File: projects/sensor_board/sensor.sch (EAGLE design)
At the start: 63 parts, among them J1 504050-0791, J2 FH28-10S-0.5SH_05_, J3 504050-0791, J4 504050-1091, J5 504050-0791, J6 504050-0791, U1 NXP_FXAS21002CQR1_EDITEDNXP_F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, U2 HONEYWELL_HMC5983-TRHONEYWELL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, U3 DS1307N, U4 NXP_FXAS21002CQR1_EDITEDNXP_F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, U5 HONEYWELL_HMC5983-TRHONEYWELL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, U6 NXP_FXAS21002CQR1_EDITEDNXP_F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, U7 HONEYWELL_HMC5983-TRHONEYWELL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, Y1 ECS-.327-12.5-13X

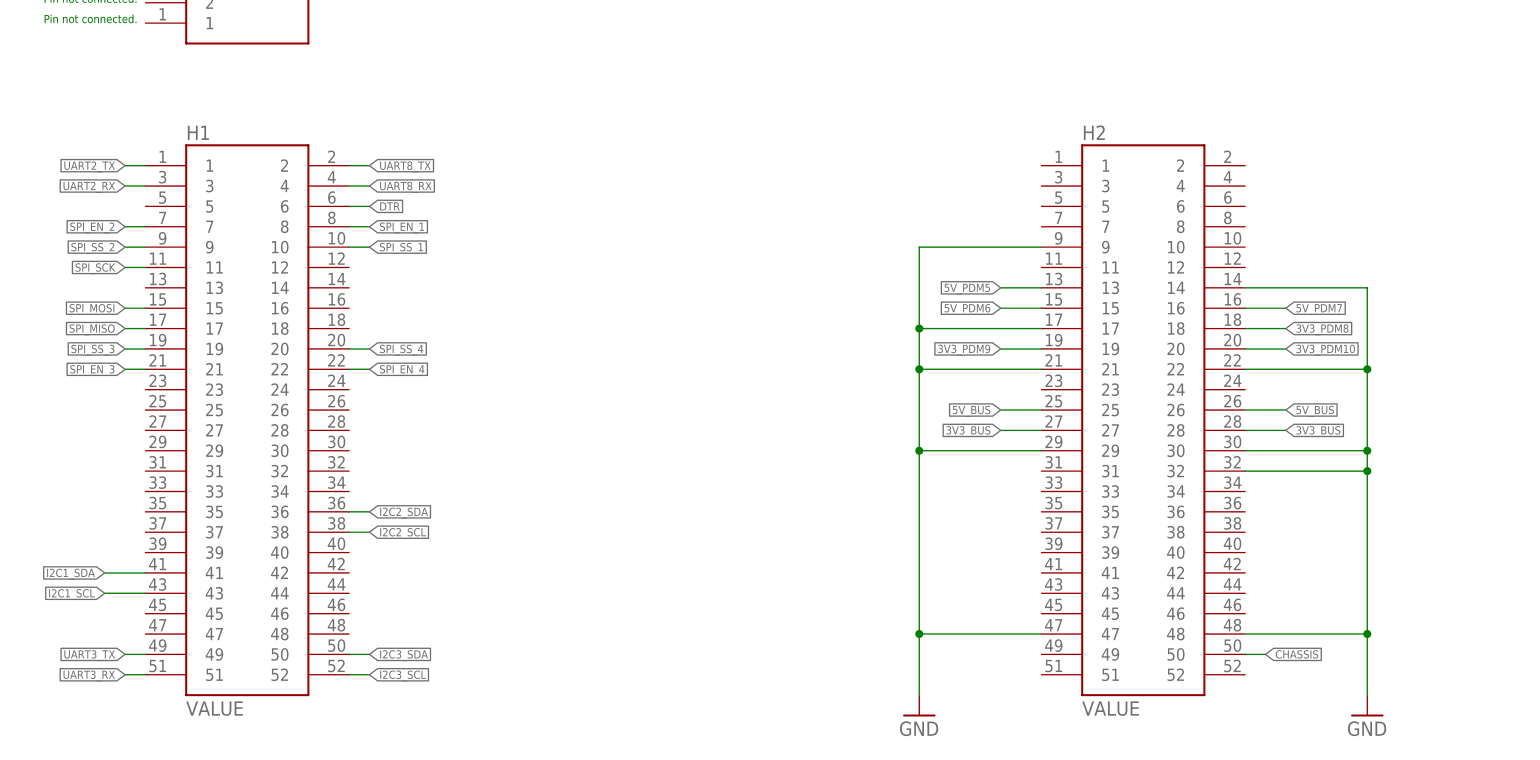
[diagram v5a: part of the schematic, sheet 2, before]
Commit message: sensor board updated
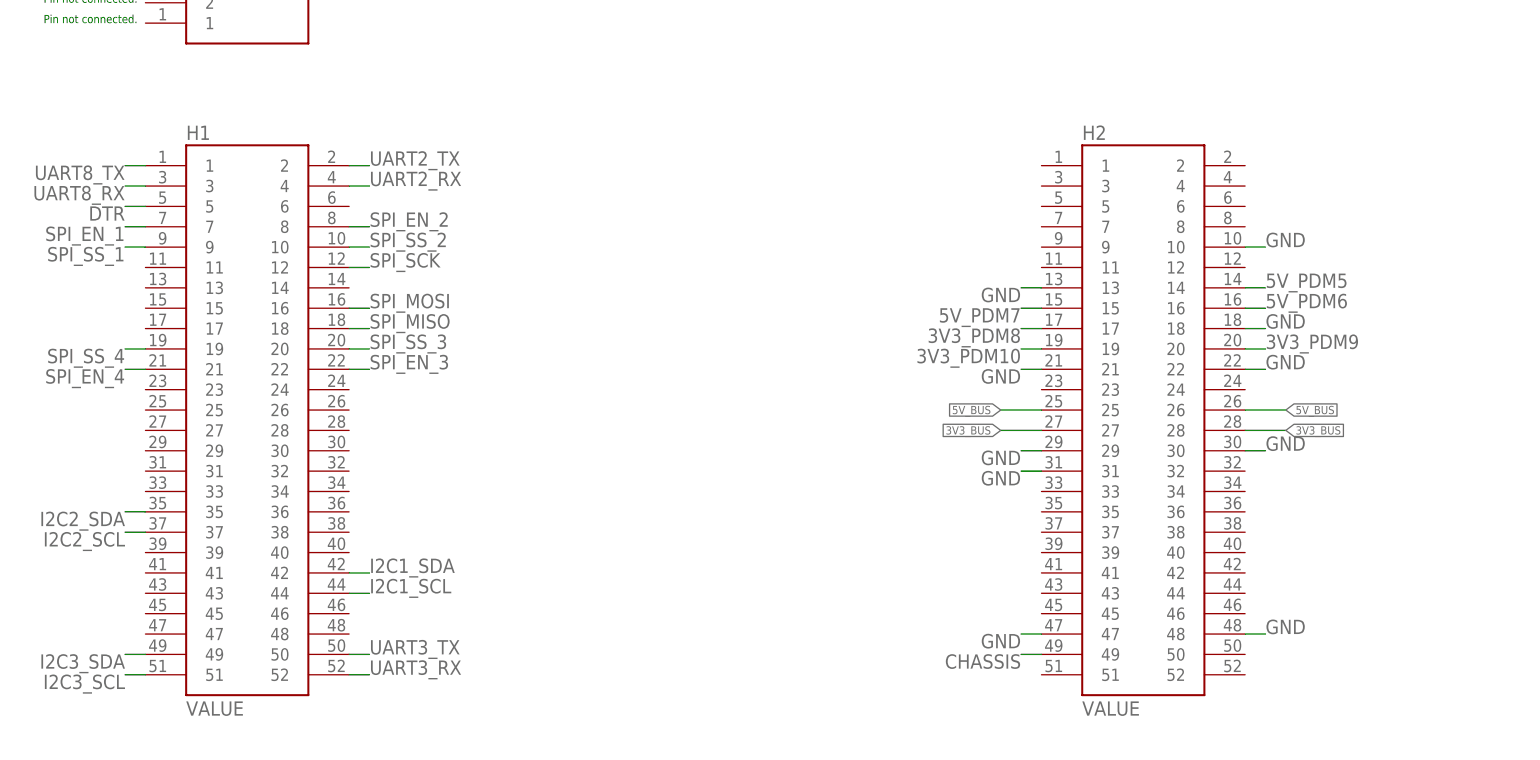
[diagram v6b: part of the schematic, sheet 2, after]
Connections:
- net 3V3_PDM10: now also H2.19; no longer H2.20
- net 3V3_PDM8: now also H2.17; no longer H2.18
- net 3V3_PDM9: now also H2.20; no longer H2.19
- net 5V_PDM5: now also H2.14; no longer H2.13
- net 5V_PDM6: now also H2.16; no longer H2.15
- net 5V_PDM7: now also H2.15; no longer H2.16
- net CHASSIS: now also H2.49; no longer H2.50
- net DTR: now also H1.5; no longer H1.6
- net GND: now also H2.10, H2.13, H2.18, H2.31; no longer H2.14, H2.17, H2.32, H2.9
- net I2C1_SCL: now also H1.44; no longer H1.43
- net I2C1_SDA: now also H1.42; no longer H1.41
- net I2C2_SCL: now also H1.37; no longer H1.38
- net I2C2_SDA: now also H1.35; no longer H1.36
- net I2C3_SCL: now also H1.51; no longer H1.52
- net I2C3_SDA: now also H1.49; no longer H1.50
- net SPI_EN_1: now also H1.7; no longer H1.8
- net SPI_EN_2: now also H1.8; no longer H1.7
- net SPI_EN_3: now also H1.22; no longer H1.21
- net SPI_EN_4: now also H1.21; no longer H1.22
- net SPI_MISO: now also H1.18; no longer H1.17
- net SPI_MOSI: now also H1.16; no longer H1.15
- net SPI_SCK: now also H1.12; no longer H1.11
- net SPI_SS_1: now also H1.9; no longer H1.10
- net SPI_SS_2: now also H1.10; no longer H1.9
- net SPI_SS_3: now also H1.20; no longer H1.19
- net SPI_SS_4: now also H1.19; no longer H1.20
- net UART2_RX: now also H1.4; no longer H1.3
- net UART2_TX: now also H1.2; no longer H1.1
- net UART3_RX: now also H1.52; no longer H1.51
- net UART3_TX: now also H1.50; no longer H1.49
- net UART8_RX: now also H1.3; no longer H1.4
- net UART8_TX: now also H1.1; no longer H1.2

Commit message: Update sensor.sch
Updated with fix to I2C lines
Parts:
- removed C17, C9: 1.0 uF, rcl:C-USC0805
- removed LED2, LED3, LED4: (no value), led:LEDCHIP-LED0805
- removed R1, R16, R2, R9: 4.7k, ngspice-simulation:R
- removed R11, R13, R17, R18, R3, R4: 2.2k, ngspice-simulation:R
- removed R6, R7, R8: (no value), rcl:R-US_R0805
- removed U2, U5, U7: HONEYWELL_HMC5983-TRHONEYWELL_HMC5983-TR_0_0, Honeywell - HMC5983-TR:HONEYWELL_HMC5983-TRHONEYWELL_HMC5983-TR_0_0
- added ADC: ADC128D818CIMT/NOPB, ADC128D818CIMT_NOPB:ADC128D818CIMT/NOPB
- added C25: C1206X104K5RAC3316, SamacSys_Parts:C1206X104K5RAC3316
- added C26, C27: EMF325B7106KMHP, SamacSys_Parts:EMF325B7106KMHP
- added C33: C1206X475K3RACAUTO7210, SamacSys_Parts:C1206X475K3RACAUTO7210
- added IC1: TSX634AIYPT, SamacSys_Parts:TSX634AIYPT
- added IC2, IC3, IC6: LSM303DLHC, st-microelectronics:LSM303DLHC
- added IC4: OPA991IDBVR, SamacSys_Parts:OPA991IDBVR
- added J10, J7, J8, J9: DF13A-2P-1.25H_21_, SamacSys_Parts:DF13A-2P-1.25H_21_
- added LED5, LED6, LED8: LG_R971-KN-1, SamacSys_Parts:LG_R971-KN-1
- added R19: PTN0402Y1002BST1, SamacSys_Parts:PTN0402Y1002BST1
- added R20: PMR01ZZPJ000, SamacSys_Parts:PMR01ZZPJ000
- added R21, R22, R23: CR0402-FX-1400GLF, SamacSys_Parts:CR0402-FX-1400GLF
- added R31, R32, R33, R34, R35, R36: RS73G1JTTD4701B, SamacSys_Parts:RS73G1JTTD4701B
- BT1: device BA2032SM:BA2032SM -> BA2032SM_PAD_replace:BA2032SM
- C1: value 1.0 uF -> C1206X104K5RAC3316; device rcl:C-USC0805 -> SamacSys_Parts:C1206X104K5RAC3316
- C10, C13, C18, C2, C20, C3, C5: value 0.1 uF -> C1206X104K5RAC3316; device rcl:C-USC0805 -> SamacSys_Parts:C1206X104K5RAC3316
- C11, C12: value 0.1 uF -> C0805F224M5RACAUTO7210; device rcl:C-USC0805 -> SamacSys_Parts:C0805F224M5RACAUTO7210
- C14, C22: value 0.22 uF -> C1206X104K5RAC3316; device rcl:C-USC0805 -> SamacSys_Parts:C1206X104K5RAC3316
- C15: value 4.7 uF -> EMF325B7106KMHP; device rcl:C-USC0805 -> SamacSys_Parts:EMF325B7106KMHP
- C16: value 100 nF -> C1206X104K5RAC3316; device rcl:C-USC0805 -> SamacSys_Parts:C1206X104K5RAC3316
- C19, C21, C4: value 0.1 uF -> CGAEB1X7T0G105M050BC; device rcl:C-USC0805 -> SamacSys_Parts:CGAEB1X7T0G105M050BC
- C23: value 4.7 uF -> C1206X104K5RAC3316; device rcl:C-USC0805 -> SamacSys_Parts:C1206X104K5RAC3316
- C24: value 100 nF -> CGAEB1X7T0G105M050BC; device rcl:C-USC0805 -> SamacSys_Parts:CGAEB1X7T0G105M050BC
- C6: value 0.22 uF -> C1206X475K3RACAUTO7210; device rcl:C-USC0805 -> SamacSys_Parts:C1206X475K3RACAUTO7210
- C7: value 100 nF -> C1206X475K3RACAUTO7210; device rcl:C-USC0805 -> SamacSys_Parts:C1206X475K3RACAUTO7210
- C8: value 4.7 uF -> C0805F224M5RACAUTO7210; device rcl:C-USC0805 -> SamacSys_Parts:C0805F224M5RACAUTO7210
- LED1: value (none) -> LH_R974-LP-1; device led:LEDCHIP-LED0805 -> SamacSys_Parts:LH_R974-LP-1
- R10, R12, R14, R15: value 4.7k -> PTN0402Y1002BST1; device ngspice-simulation:R -> SamacSys_Parts:PTN0402Y1002BST1
- R5: value (none) -> RN73H2ATTD75R0B25; device rcl:R-US_R0805 -> SamacSys_Parts:RN73H2ATTD75R0B25
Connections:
- removed net N$45: C6.2, U2.SETC
- removed net N$46: C6.1, U2.SETP
- removed net N$47: C14.2, U5.SETC
- removed net N$48: C14.1, U5.SETP
- removed net N$49: C22.2, U7.SETC
- removed net N$50: C22.1, U7.SETP
- removed net N$51: C15.1, U5.C1
- removed net N$52: C8.1, U2.C1
- removed net N$56: C23.1, U7.C1
- new net ADCIN0: ADC.IN0, IC1.OUT1, R12.1
- new net ADCIN1: ADC.IN1, IC1.OUT2, R14.1
- new net ADCIN2: ADC.IN2, IC1.OUT3, R15.1
- new net ADCIN3: ADC.IN3, IC1.OUT4, R19.1
- new net ADCIN4: ADC.IN4, IC4.OUT, R10.1
- new net CHASSIS_CONNECTION: R20.2
- new net N$10: C8.2, IC3.SETC
- new net N$11: C11.1, IC2.SETP
- new net N$12: C11.2, IC2.SETC
- new net N$13: C7.1, IC2.C1
- new net N$14: C12.1, IC6.SETP
- new net N$15: C12.2, IC6.SETC
- new net N$16: C33.1, IC6.C1
- new net N$8: C6.1, IC3.C1
- new net N$9: C8.1, IC3.SETP
- new net PH1_POS: IC1.IN1-, J8.1, R12.2
- new net PH2_POS: IC1.IN2-, J10.1, R14.2
- new net PH3_POS: IC1.IN3-, J7.1, R15.2
- new net PH4_POS: IC1.IN4-, J9.1, R19.2
- new net PH5_POS: H1.36, IC4.IN-, R10.2
- net 3V3_PDM9: now also ADC.V+, ADC.VREF, C14.1, C15.1, C19.2, C21.2, C22.1, C23.1, C24.2, C25.1, C26.1, C27.1, C3.2, IC1.VCC+, IC2.VDD, IC2.VDD_IO, IC3.VDD, IC3.VDD_IO, IC4.V+, IC6.VDD, IC6.VDD_IO, J2.1, J2.2, LED1.A, R31.2, R32.2, R33.2, R34.2, R35.2, R36.2; no longer C1.1, C10.1, C11.1, C12.1, C17.1, C19.1, C21.1, C3.1, C9.1, J2.6, LED4.A, R1.2, R10.2, R11.2, R13.1, R15.2, R16.2, R17.2, R18.1, R2.2, R3.2, R4.1, R9.2, U2.!SPI_CS!(S1), U2.I2C/!SPI!, U2.VDD, U2.VDDIO, U5.!SPI_CS!(S1), U5.I2C/!SPI!, U5.VDD, U5.VDDIO, U7.!SPI_CS!(S1), U7.I2C/!SPI!, U7.VDD, U7.VDDIO
- net 5V_BUS: no longer R12.1, R14.1
- net 5V_PDM5: now also LED5.A; no longer J4.3, LED1.A
- net 5V_PDM6: now also LED6.A; no longer LED2.A
- net 5V_PDM7: now also J4.8, LED8.A; no longer LED3.A
- net CHASSIS: now also J2.3; no longer J2.7
- net DTR: now also J4.5; no longer J4.6
- net GND: now also ADC.GND, C14.2, C19.1, C21.1, C22.2, C24.1, C25.2, C26.2, C27.2, C3.1, C33.2, C6.2, H1.38, IC1.IN1+, IC1.IN2+, IC1.IN3+, IC1.IN4+, IC1.VCC-, IC2.GND, IC2.RSVD@1, IC2.RSVD@2, IC3.GND, IC3.RSVD@1, IC3.RSVD@2, IC4.IN+, IC4.V-, IC6.GND, IC6.RSVD@1, IC6.RSVD@2, J10.2, J2.4, J2.5, J4.2, J7.2, J8.2, J9.2, R20.1, R21.1, R22.1, R23.1; no longer C11.2, C12.2, C17.2, C19.2, C21.2, C24.2, C3.2, C8.2, C9.2, J2.10, J2.8, J2.9, J4.4, J4.5, R6.1, R7.1, R8.1, U2.GND, U2.SOC, U5.GND, U5.SOC, U7.GND, U7.SOC
- net I2C1_SCL: now also IC6.SLC, R32.1; no longer R14.2, R16.1, R17.1, U7.SCL/SPI_SCK
- net I2C1_SDA: now also IC6.SDA, R31.1; no longer R12.2, R15.1, R18.2, U7.SDA/SPI_SDI
- net I2C2_SCL: now also ADC.SCL, IC2.SLC, R34.1; no longer R2.1, R3.1, U2.SCL/SPI_SCK
- net I2C2_SDA: now also ADC.SDA, IC2.SDA, R33.1; no longer R1.1, R4.2, U2.SDA/SPI_SDI
- net I2C3_SCL: now also IC3.SLC, J4.6, R36.1; no longer J4.9, R10.1, R11.1, U5.SCL/SPI_SCK
- net I2C3_SDA: now also IC3.SDA, J4.7, R35.1; no longer J4.10, R13.2, R9.1, U5.SDA/SPI_SDI
- net N$1: now also LED5.K, R21.2; no longer LED1.C, R5.2
- net N$2: now also LED6.K, R22.2; no longer LED2.C, R6.2
- net N$3: now also LED8.K, R23.2; no longer LED3.C, R7.2
- net N$4: now also LED1.K, R5.2; no longer LED4.C, R8.2
- net N$67: now also C10.1; no longer C16.1
- net N$71: now also C1.1; no longer C7.1
- net N$72: now also C16.1; no longer C24.1
- net UART3_RX: now also J2.7; no longer J2.5
- net UART3_TX: now also J2.8; no longer J2.3
- net UART8_RX: now also J4.4; no longer J4.8
- net UART8_TX: now also J4.3; no longer J4.7
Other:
- note removed: "Pin not connected."
- moved on the sheet: BT1, H1, H2, J1, J2, J3, J4, J5, J6, LED1, U3, U4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
